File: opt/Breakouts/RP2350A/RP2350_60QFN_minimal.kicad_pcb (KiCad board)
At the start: 2 copper layers, 52 x 51 mm, 43 parts, among them J1 USB_B_Micro, J2 Conn_02x18_Odd_Even, J3 Conn_02x18_Odd_Even, J4 SM03B-SRSS-TB, SW1 SW_Push, SW2 SW_Push, U1 RP2350_60QFN, U2 NCP1117-3.3_SOT223, U3 W25Q128JVS, Y1 ABM8-272-T3

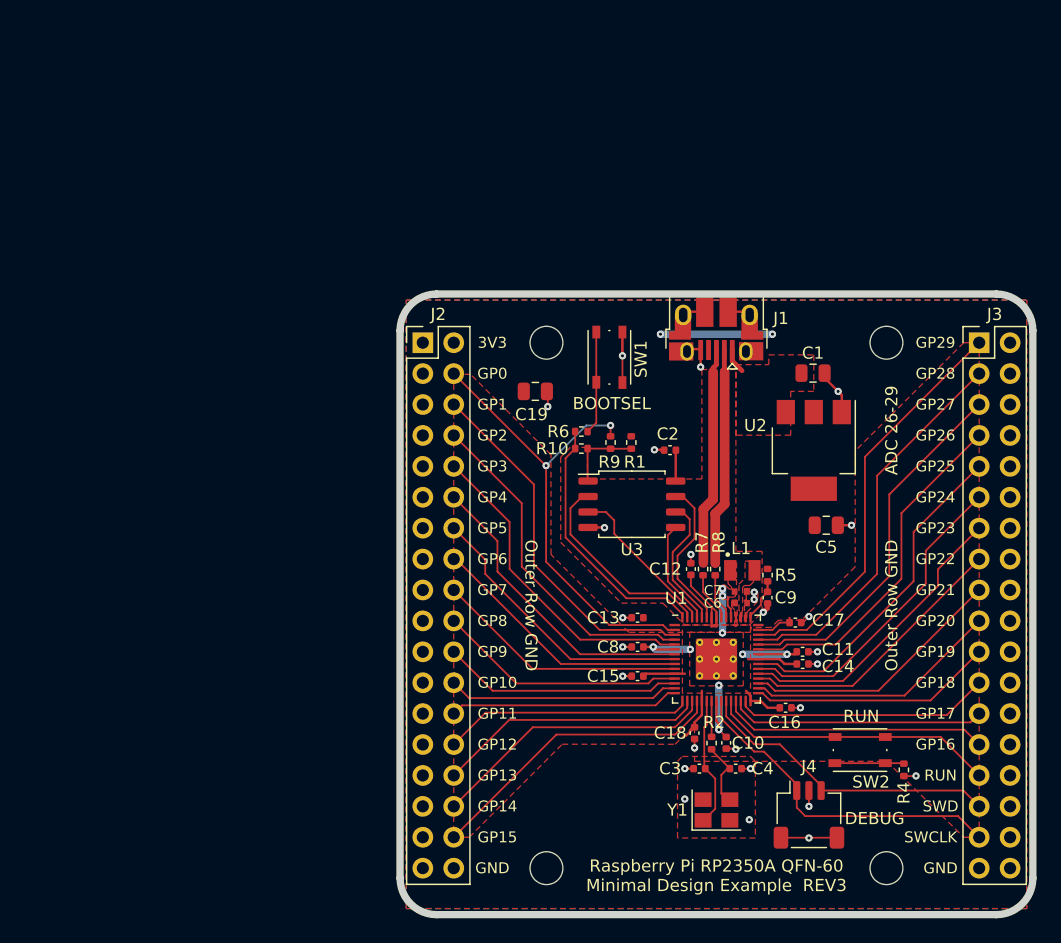
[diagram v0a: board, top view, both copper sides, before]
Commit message: Finished building the RP2350 module
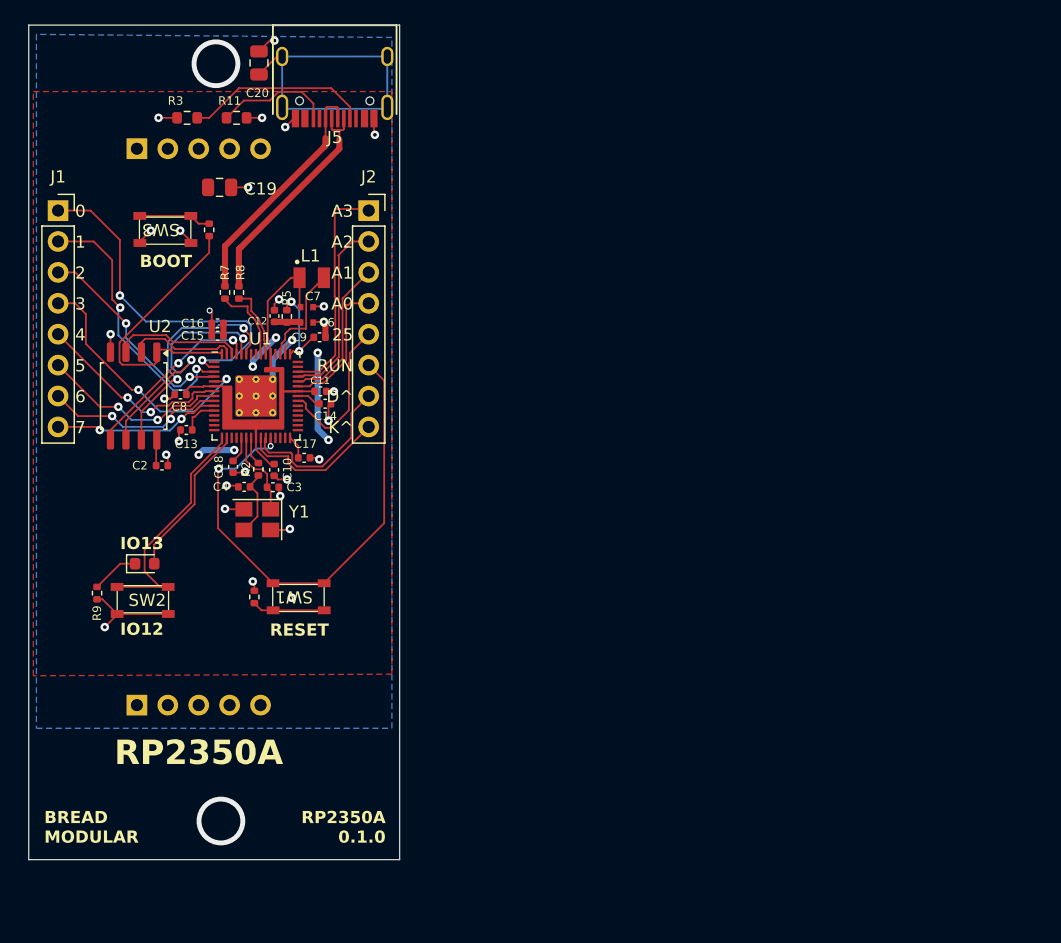
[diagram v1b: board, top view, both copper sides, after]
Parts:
- removed C1, C5: 10u, Capacitor_SMD:C_0805_2012Metric
- removed H1, H2, H3, H4: MountingHole, MountingHole:MountingHole_2.7mm_M2.5
- removed J3: Conn_02x18_Odd_Even, Connector_PinHeader_2.54mm:PinHeader_2x18_P2.54mm_Vertical
- removed J4: SM03B-SRSS-TB, Connector_JST:JST_SH_SM03B-SRSS-TB_1x03-1MP_P1.00mm_Horizontal
- removed R1: DNF, Resistor_SMD:R_0402_1005Metric
- removed R10: 0, Resistor_SMD:R_0402_1005Metric
- removed U3: W25Q128JVS, Package_SO:SOIC-8_5.23x5.23mm_P1.27mm
- added C20: 10nf, Capacitor_SMD:C_0805_2012Metric, F.Cu at (65.9, 43.7)
- added D1: LED, LED_SMD:LED_0603_1608Metric, F.Cu at (56.5, 84.9)
- added GND1: Conn_01x05_Pin, Connector_PinHeader_2.54mm:PinHeader_1x05_P2.54mm_Vertical, B.Cu at (55.9, 96.5)
- added J5: USB_C_Receptacle_USB2.0_14P, BreadModular_TypeC:HRO-TYPE-C-31-M-12, F.Cu at (72.1, 40.6)
- added R11: 5.1k, Resistor_SMD:R_0603_1608Metric, F.Cu at (64.1, 48.3)
- added R3: 5.1k, Resistor_SMD:R_0603_1608Metric, F.Cu at (60.0, 48.3)
- added SW3: K2-1808SN-A4SW-01, BreadModular_MISC:K2-1808SN-A4SW-01, F.Cu at (58.3, 57.4)
- added V_SUPPLY1: Conn_01x05_Pin, Connector_PinHeader_2.54mm:PinHeader_1x05_P2.54mm_Vertical, B.Cu at (55.9, 50.8)
- J1: value USB_B_Micro -> Conn_01x08_Socket; footprint Connector_USB:USB_Micro-B_Amphenol_10103594-0001LF_Horizontal -> Connector_PinSocket_2.54mm:PinSocket_1x08_P2.54mm_Vertical
- J2: value Conn_02x18_Odd_Even -> Conn_01x08_Socket; footprint Connector_PinHeader_2.54mm:PinHeader_2x18_P2.54mm_Vertical -> Connector_PinSocket_2.54mm:PinSocket_1x08_P2.54mm_Vertical
- L1: value 3.3u -> AOTA-B201610S3R3-101-T
- R9: value DNF -> 1k
- SW1: value SW_Push -> SW_SPST; footprint Button_Switch_SMD:SW_Push_1P1T_NO_Vertical_Wuerth_434133025816 -> BreadModular_MISC:K2-1808SN-A4SW-01
- SW2: value SW_Push -> K2-1808SN-A4SW-01; footprint Button_Switch_SMD:SW_Push_1P1T_NO_Vertical_Wuerth_434133025816 -> BreadModular_MISC:K2-1808SN-A4SW-01
- U2: value NCP1117-3.3_SOT223 -> W25Q128JVS; footprint Package_TO_SOT_SMD:SOT-223-3_TabPin2 -> Package_SO:SOIC-8_5.23x5.23mm_P1.27mm
- moved SW2 60.3 mm to (56.3, 87.9), turned to 0 degrees
- moved C16 56.4 mm to (62.5, 65.2), turned to 180 degrees
- moved U2 56.1 mm to (55.6, 71.1)
- moved R4 55.2 mm to (65.5, 87.6), turned to 90 degrees
- moved J1 54.9 mm to (49.4, 55.9), turned to 0 degrees
- moved C4 46.6 mm to (64.7, 78.6), turned to 180 degrees
- moved R7 45.4 mm to (63.1, 62.6)
- moved R8 45.3 mm to (64.3, 62.6)
- moved C11 45.0 mm to (71.0, 70.7)
- moved R5 44.9 mm to (68.2, 64.6), turned to 90 degrees
- moved C14 44.7 mm to (71.4, 71.8)
- moved Y1 44.6 mm to (65.8, 81.3), turned to 180 degrees
- moved C15 44.4 mm to (62.5, 66.2)
- moved R9 44.0 mm to (52.6, 87.3), turned to 90 degrees
- moved C18 43.8 mm to (63.8, 76.9)
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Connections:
- J1 pad 1: VBUS -> /GPIO0
- J1 pad 2: /USB_D- -> /GPIO1
- J1 pad 3: /USB_D+ -> /GPIO2
- J1 pad 4: unconnected-(J1-ID-Pad4) -> /GPIO3
- J1 pad 5: GND -> /GPIO4
- J1 pad 6: GND -> /GPIO5
- J2 pad 1: GND -> /GPIO29_ADC3
- J2 pad 2: +3V3 -> /GPIO28_ADC2
- J2 pad 3: GND -> /GPIO27_ADC1
- J2 pad 4: /GPIO0 -> /GPIO26_ADC0
- J2 pad 5: GND -> /GPIO25
- J2 pad 6: /GPIO1 -> /RUN
- J2 pad 7: GND -> /SWD
- J2 pad 8: /GPIO2 -> /SWCLK
- R4 pad 1: Net-(R4-Pad1) -> Net-(SW1-A)
- R6 pad 1: /QSPI_SS -> QSPI_SS
- R7 pad 1: /USB_D+ -> USB_D+
- R8 pad 1: /USB_D- -> USB_D-
- R9 pad 1: /GPIO0 -> GND
- R9 pad 2: /FLASH_SS -> Net-(D1-K)
- SW1 pad 1: GND -> Net-(SW1-A)
- SW1 pad 2: /~{USB_BOOT} -> /RUN
- SW2 pad 1: Net-(R4-Pad1) -> /GPIO12
- SW2 pad 2: /RUN -> GND
- U1 pad 12: /GPIO8 -> unconnected-(U1-GPIO8-Pad12)
- U1 pad 13: /GPIO9 -> unconnected-(U1-GPIO9-Pad13)
- U1 pad 14: /GPIO10 -> unconnected-(U1-GPIO10-Pad14)
- U1 pad 15: /GPIO11 -> unconnected-(U1-GPIO11-Pad15)
- U1 pad 18: /GPIO14 -> unconnected-(U1-GPIO14-Pad18)
- U1 pad 19: /GPIO15 -> unconnected-(U1-GPIO15-Pad19)
- U1 pad 27: /GPIO16 -> unconnected-(U1-GPIO16-Pad27)
- U1 pad 28: /GPIO17 -> unconnected-(U1-GPIO17-Pad28)
- U1 pad 29: /GPIO18 -> unconnected-(U1-GPIO18-Pad29)
- U1 pad 31: /GPIO19 -> unconnected-(U1-GPIO19-Pad31)
- U1 pad 32: /GPIO20 -> unconnected-(U1-GPIO20-Pad32)
- U1 pad 33: /GPIO21 -> unconnected-(U1-GPIO21-Pad33)
- U1 pad 34: /GPIO22 -> unconnected-(U1-GPIO22-Pad34)
- U1 pad 35: /GPIO23 -> unconnected-(U1-GPIO23-Pad35)
- U1 pad 36: /GPIO24 -> unconnected-(U1-GPIO24-Pad36)
- U1 pad 60: /QSPI_SS -> QSPI_SS
- U2 pad 1: GND -> QSPI_SS
- U2 pad 2: +3V3 -> /QSPI_SD1
- U2 pad 3: VBUS -> /QSPI_SD2
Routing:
- net Net-(J5-SHIELD): track 0.00 -> 28.3 mm
- net /GPIO24: track 26.1 -> 0.00 mm
- net /GPIO15: track 25.2 -> 0.00 mm
- net /GPIO23: track 24.4 -> 0.00 mm
- net /GPIO14: track 23.6 -> 0.00 mm
- net QSPI_SS: track 0.00 -> 23.0 mm
- net GND: track 37.5 -> 60.2 mm, vias 27 -> 29
- net /GPIO22: track 22.7 -> 0.00 mm
- net /GPIO16: track 22.0 -> 0.00 mm
- net /GPIO21: track 21.8 -> 0.00 mm
- net /QSPI_SS: track 21.5 -> 0.00 mm
- net /GPIO18: track 21.0 -> 0.00 mm
- net /GPIO17: track 21.0 -> 0.00 mm
- net /GPIO20: track 20.9 -> 0.00 mm
- net /GPIO8: track 20.4 -> 0.00 mm
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- removed copper zone on F.Cu, net +1V1
- removed copper zone on F.Cu, net /VREG_LX
- removed copper zone on F.Cu, net GND
- removed copper zone on F.Cu, net VBUS
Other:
- board size 52 x 51 mm -> 30.5 x 68.6 mm
- rule pad_to_mask_clearance: 0.051 -> 0
- board text added: "0"
- board text added: "1"
- board text added: "2"
- board text added: "25"
- board text added: "3"
- board text added: "4"
- board text added: "5"
- board text added: "6"
- board text added: "7"
- board text added: "A0"
- board text added: "A1"
- board text added: "A2"
- board text added: "A3"
- board text added: "BOOT"
- board text added: "BREAD MODULAR"
- board text added: "D^"
- board text added: "IO12"
- board text added: "IO13"
- board text added: "K^"
- board text added: "RESET"
- board text added: "RP2350A"
- board text added: "RP2350A 0.1.0"
- board text removed: "3V3"
- board text removed: "ADC 26-29"
- board text removed: "BOOTSEL"
- board text removed: "DEBUG"
- board text removed: "GND"
- board text removed: "GP0"
- board text removed: "GP1"
- board text removed: "GP10"
- board text removed: "GP11"
- board text removed: "GP12"
- board text removed: "GP13"
- board text removed: "GP14"
- board text removed: "GP15"
- board text removed: "GP16"
- board text removed: "GP17"
- board text removed: "GP18"
- board text removed: "GP19"
- board text removed: "GP2"
- board text removed: "GP20"
- board text removed: "GP21"
- board text removed: "GP22"
- board text removed: "GP23"
- board text removed: "GP24"
- board text removed: "GP25"
- board text removed: "GP26"
- board text removed: "GP27"
- board text removed: "GP28"
- board text removed: "GP29"
- board text removed: "GP3"
- board text removed: "GP4"
- board text removed: "GP5"
- board text removed: "GP6"
- board text removed: "GP7"
- board text removed: "GP8"
- board text removed: "GP9"
- board text removed: "Minimal Design Example REV3"
- board text removed: "Outer Row GND"
- board text removed: "Raspberry Pi RP2350A QFN-60"
- board text removed: "SWCLK"
- board text removed: "SWD"

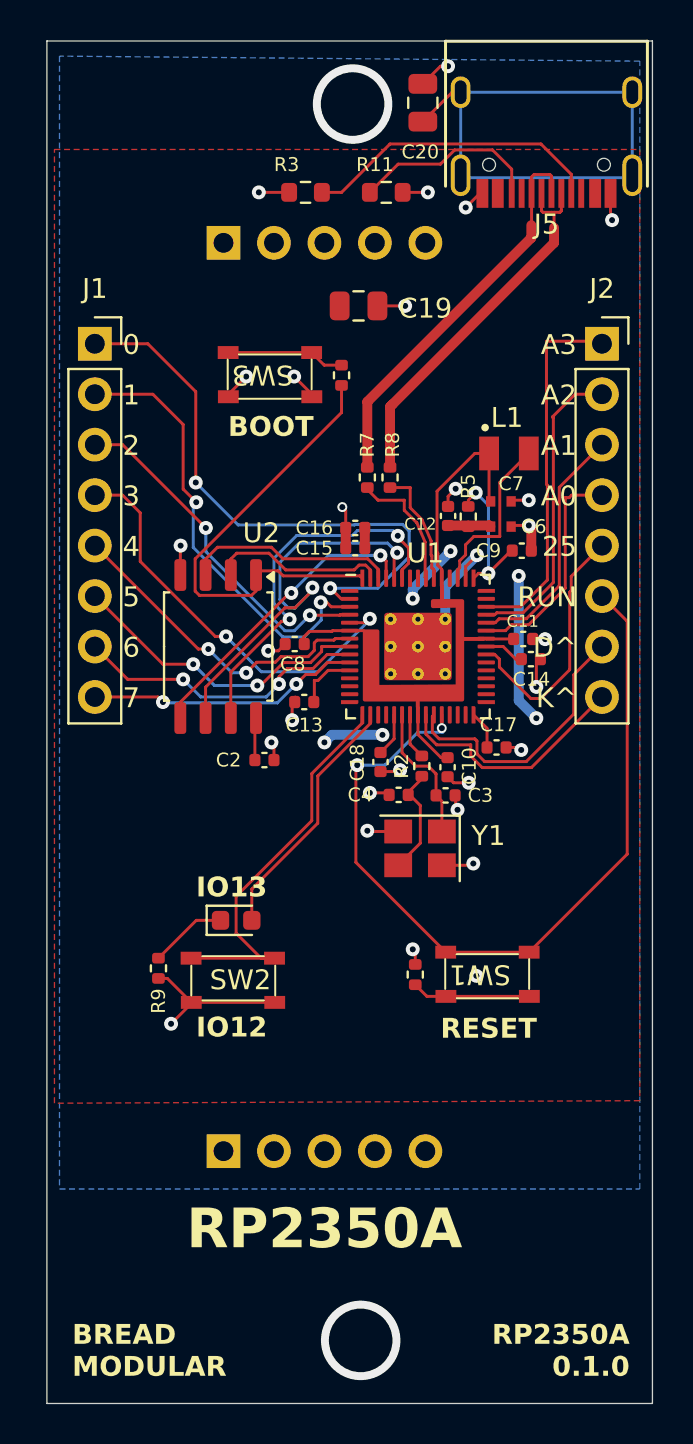
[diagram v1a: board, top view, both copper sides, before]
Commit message: Add the initial version of 16bit
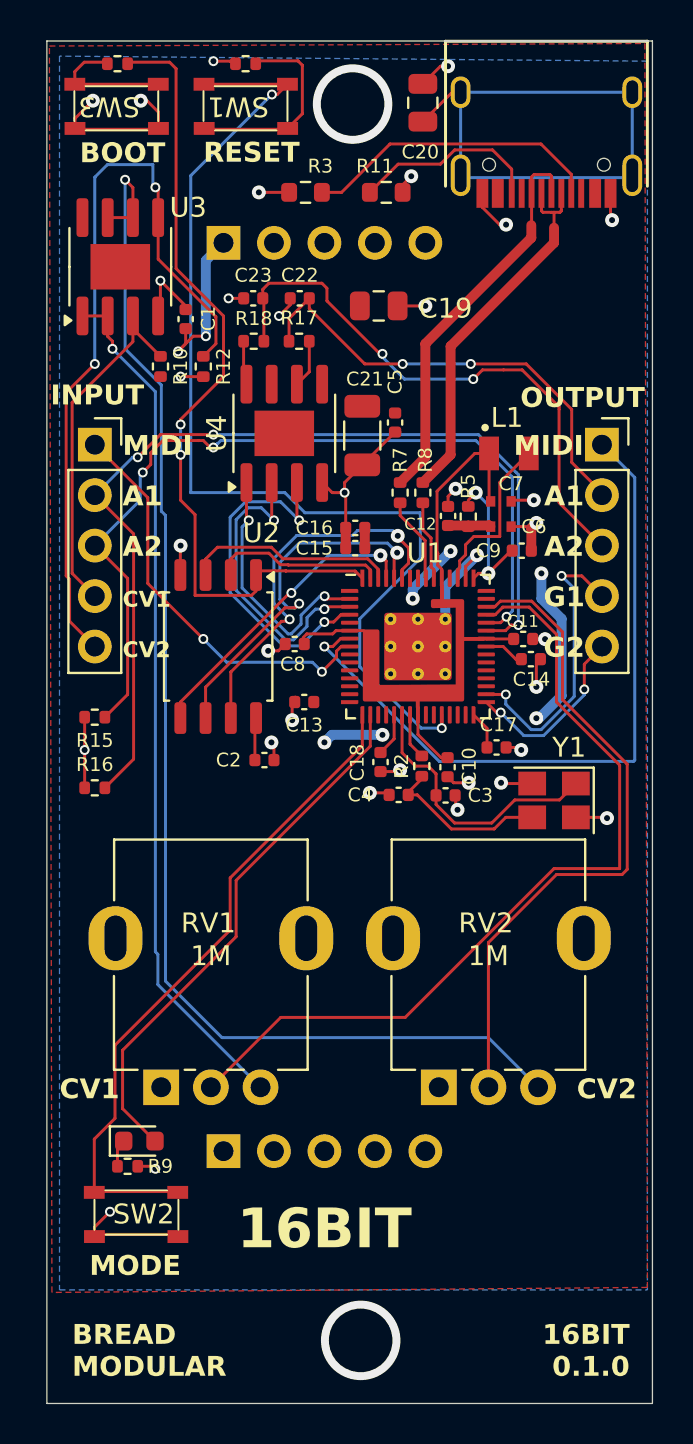
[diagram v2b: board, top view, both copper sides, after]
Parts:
- added C1: 0.1uf, Capacitor_SMD:C_0402_1005Metric, F.Cu at (54.0, 54.6)
- added C21: 100uf, Capacitor_SMD:C_1206_3216Metric, F.Cu at (62.9, 60.5)
- added C22: 10nf, Capacitor_SMD:C_0402_1005Metric, F.Cu at (59.7, 53.6)
- added C23: 10nf, Capacitor_SMD:C_0402_1005Metric, F.Cu at (57.4, 53.6)
- added C5: 0.1uf, Capacitor_SMD:C_0402_1005Metric, F.Cu at (64.5, 59.8)
- added R10: 100k, Resistor_SMD:R_0402_1005Metric, F.Cu at (52.7, 57.0)
- added R12: 100k, Resistor_SMD:R_0402_1005Metric, F.Cu at (54.9, 57.0)
- added R15: 100k, Resistor_SMD:R_0402_1005Metric, F.Cu at (49.4, 74.7)
- added R16: 100k, Resistor_SMD:R_0402_1005Metric, F.Cu at (49.4, 78.2)
- added R17: 10k, Resistor_SMD:R_0402_1005Metric, F.Cu at (59.7, 55.8)
- added R18: 10k, Resistor_SMD:R_0402_1005Metric, F.Cu at (57.4, 55.8)
- added RV1: 1M, BreadModular_Pots:Potentiometer_RV09, F.Cu at (55.4, 86.3)
- added RV2: 1M, BreadModular_Pots:Potentiometer_RV09, F.Cu at (69.3, 86.3)
- added U3: MCP6002-xSN, Package_SO:SOIC-8-1EP_3.9x4.9mm_P1.27mm_EP2.29x3mm, F.Cu at (50.7, 52.0)
- added U4: PT8211, Package_SO:SOIC-8-1EP_3.9x4.9mm_P1.27mm_EP2.29x3mm, F.Cu at (58.9, 60.4)
- J1, J2: footprint Connector_PinSocket_2.54mm:PinSocket_1x08_P2.54mm_Vertical -> Connector_PinSocket_2.54mm:PinSocket_1x05_P2.54mm_Vertical
- SW1: value SW_SPST -> K2-1808SN-A4SW-01
- moved R4 46.6 mm to (57.0, 41.8), turned to 180 degrees
- moved SW1 45.4 mm to (57.0, 43.9)
- moved R6 19.3 mm to (50.5, 41.8), turned to 180 degrees
- moved SW3 15.6 mm to (50.5, 43.9)
- moved SW2 12.8 mm to (51.4, 99.7)
- moved D1 12.1 mm to (51.6, 96.0)
- moved R9 10.1 mm to (51.1, 97.3), turned to 180 degrees
- moved Y1 7.16 mm to (72.5, 78.9)
- moved J1 5.08 mm to (49.4, 61.0)
- moved J2 5.08 mm to (74.9, 61.0)
- moved R7 1.82 mm to (64.8, 63.4)
- moved R8 1.82 mm to (65.9, 63.4)
- moved C19 1.02 mm to (63.7, 54.0)
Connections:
- J1 pad 1: /GPIO0 -> MIDI_IN
- J1 pad 2: /GPIO1 -> AIN_1
- J1 pad 3: /GPIO2 -> AIN_2
- J1 pad 4: /GPIO3 -> CV1
- J1 pad 5: /GPIO4 -> CV2
- J2 pad 1: /GPIO29_ADC3 -> MIDI_OUT
- J2 pad 2: /GPIO28_ADC2 -> AOUT_1
- J2 pad 3: /GPIO27_ADC1 -> AOUT_2
- J2 pad 4: /GPIO26_ADC0 -> GOUT_1
- J2 pad 5: /GPIO25 -> GOUT_2
- U1 pad 10: /GPIO7 -> unconnected-(U1-GPIO7-Pad10)
- U1 pad 2: /GPIO0 -> BCK
- U1 pad 24: /SWCLK -> unconnected-(U1-SWCLK-Pad24)
- U1 pad 25: /SWD -> unconnected-(U1-SWD-Pad25)
- U1 pad 3: /GPIO1 -> WS
- U1 pad 31: unconnected-(U1-GPIO19-Pad31) -> GOUT_2
- U1 pad 32: unconnected-(U1-GPIO20-Pad32) -> GOUT_1
- U1 pad 37: /GPIO25 -> unconnected-(U1-GPIO25-Pad37)
- U1 pad 4: /GPIO2 -> DIN
- U1 pad 40: /GPIO26_ADC0 -> AIN_1
- U1 pad 41: /GPIO27_ADC1 -> AIN_2
- U1 pad 42: /GPIO28_ADC2 -> BUFF_CV1
- U1 pad 43: /GPIO29_ADC3 -> BUFF_CV2
- U1 pad 5: /GPIO3 -> unconnected-(U1-GPIO3-Pad5)
- U1 pad 7: /GPIO4 -> MIDI_OUT
- U1 pad 8: /GPIO5 -> MIDI_IN
- U1 pad 9: /GPIO6 -> unconnected-(U1-GPIO6-Pad9)
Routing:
- net Net-(U3B--): track 0.00 -> 65.5 mm, vias 0 -> 1
- net AIN_1: track 0.00 -> 48.9 mm, vias 0 -> 3
- net AIN_2: track 0.00 -> 43.4 mm, vias 0 -> 3
- net Net-(U3A--): track 0.00 -> 43.3 mm, vias 0 -> 1
- net BUFF_CV1: track 0.00 -> 42.5 mm
- net CV2: track 0.00 -> 39.2 mm, vias 0 -> 2
- net MIDI_OUT: track 0.00 -> 36.0 mm, vias 0 -> 1
- net BUFF_CV2: track 0.00 -> 33.7 mm
- net /GPIO0: track 29.6 -> 0.00 mm, vias 2 -> 0
- net AOUT_2: track 0.00 -> 29.0 mm, vias 0 -> 2
- net AOUT_1: track 0.00 -> 23.4 mm, vias 0 -> 2
- net /GPIO1: track 22.7 -> 0.00 mm, vias 2 -> 0
- net GND: track 60.2 -> 81.4 mm, vias 29 -> 33
- net /GPIO3: track 21.2 -> 0.00 mm, vias 2 -> 0
- net MIDI_IN: track 0.00 -> 20.8 mm, vias 0 -> 2
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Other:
- board text added: "16BIT"
- board text added: "16BIT 0.1.0"
- board text added: "CV1"
- board text added: "CV2"
- board text added: "G1"
- board text added: "G2"
- board text added: "INPUT"
- board text added: "MIDI"
- board text added: "MODE"
- board text added: "OUTPUT"
- board text removed: "0"
- board text removed: "1"
- board text removed: "2"
- board text removed: "25"
- board text removed: "3"
- board text removed: "4"
- board text removed: "5"
- board text removed: "6"
- board text removed: "7"
- board text removed: "A0"
- board text removed: "A3"
- board text removed: "D^"
- board text removed: "IO12"
- board text removed: "IO13"
- board text removed: "K^"
- board text removed: "RP2350A"
- board text removed: "RP2350A 0.1.0"
- board text removed: "RUN"
